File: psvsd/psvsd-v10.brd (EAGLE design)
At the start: 30 x 33.4 mm, 30 parts, among them J1 TRANSFLASH-PUSH, U1 USB2244QFN, U3 VREG, Y1 24.000MHz

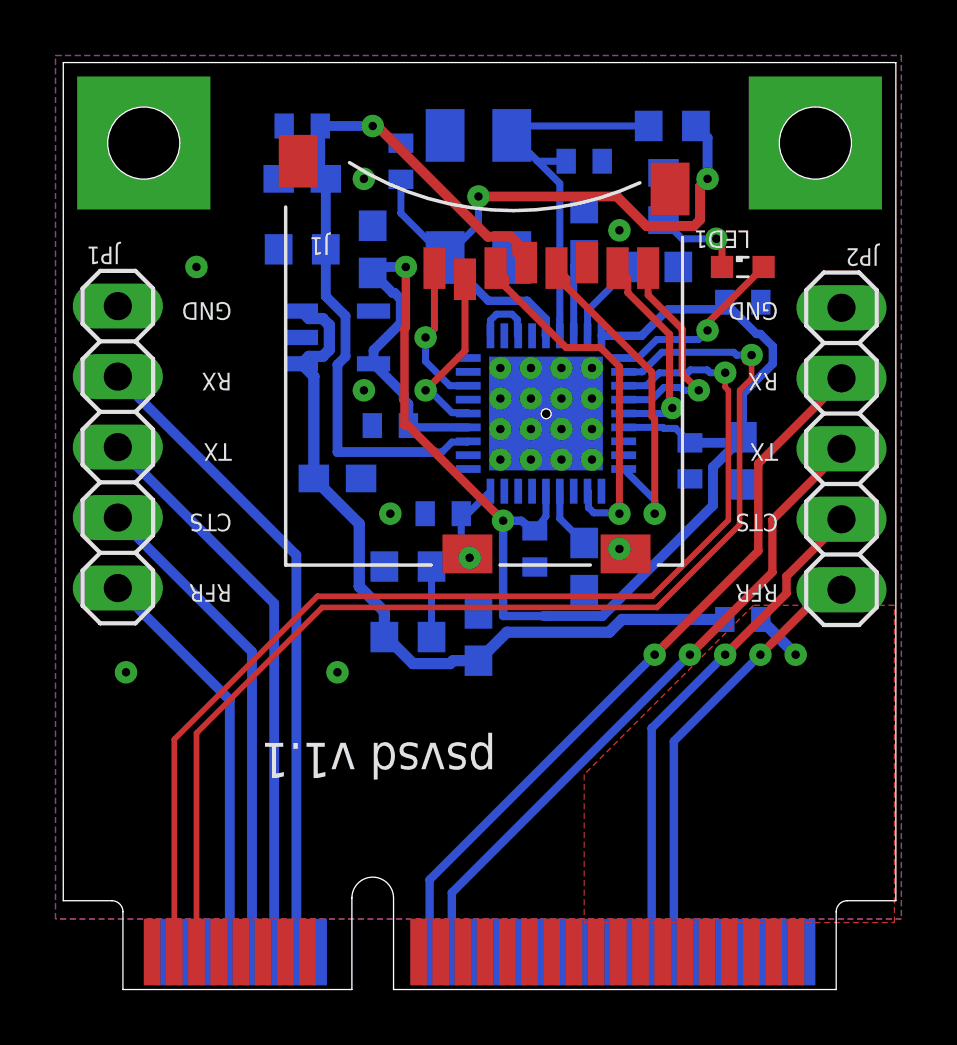
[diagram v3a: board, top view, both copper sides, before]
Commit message: Added MEM2051 part that will be used
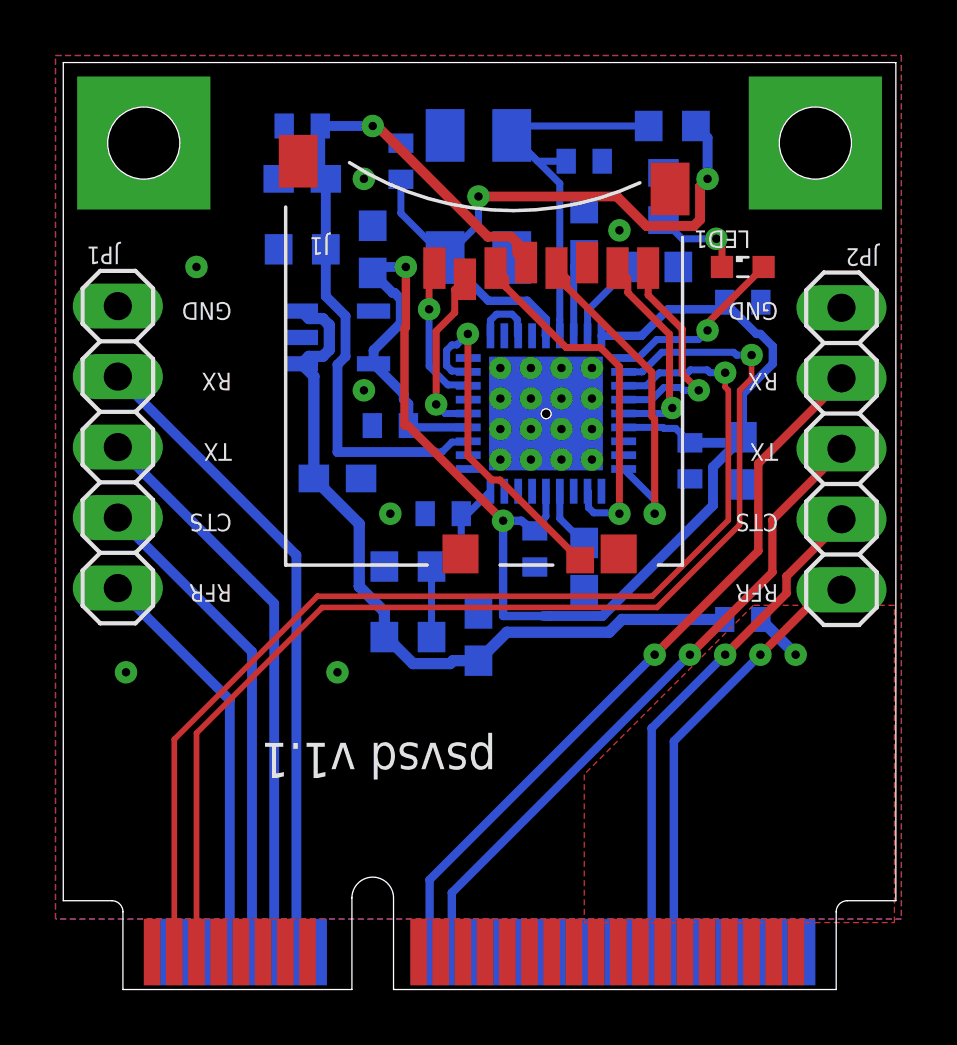
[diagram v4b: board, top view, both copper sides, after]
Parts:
- J1: value TRANSFLASH-PUSH -> MEM2051-00-195-00; device sd-mmc:MICROSD_MICROSD -> sd-mmc:MEM2051
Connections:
- new net !CD: J1.9, U1.26
- net GND: no longer J1.NC, J1.NC1, J1.NC2, J1.NC3
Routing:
- net !CD: track 0.00 -> 12.4 mm, vias 0 -> 1
- net GND: vias 25 -> 23

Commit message: Reconnected ground planes
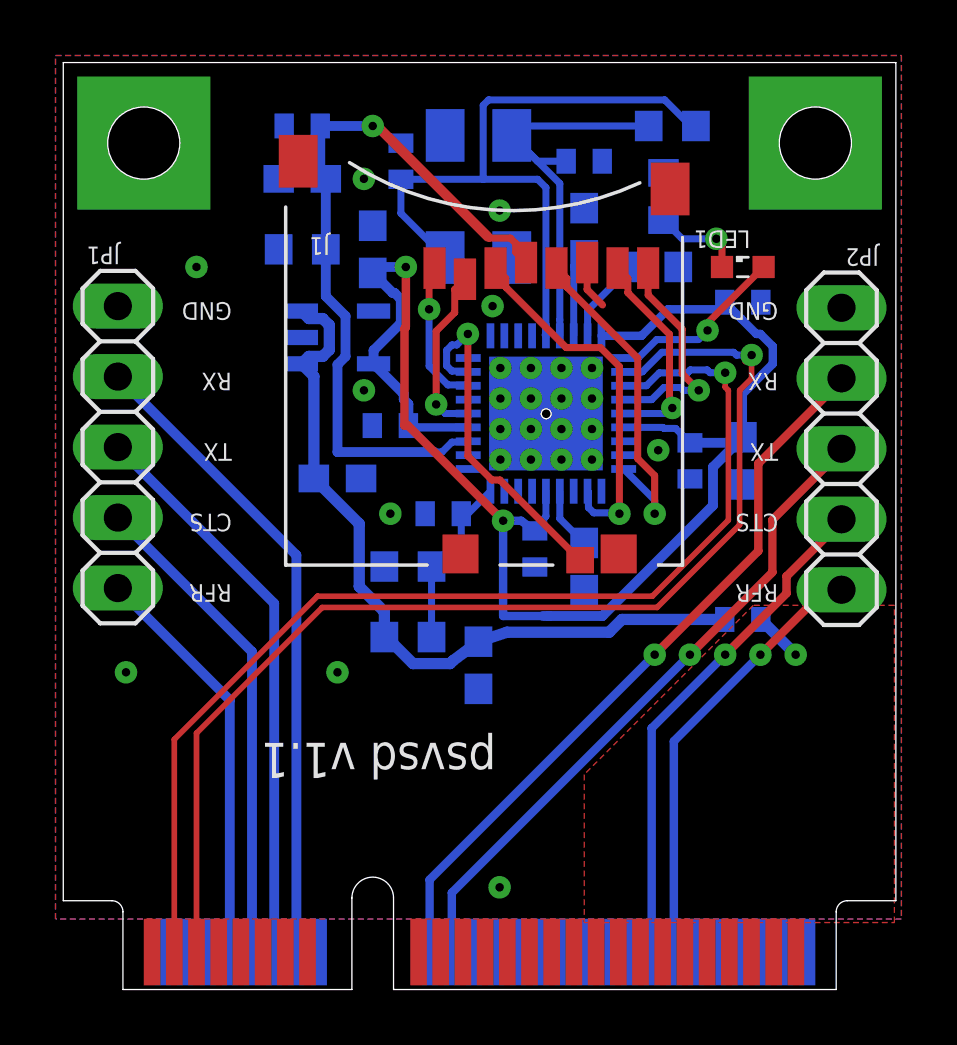
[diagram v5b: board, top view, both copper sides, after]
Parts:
- moved C5 1.02 mm to (16.5, 13.6), turned to 270 degrees
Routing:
- net XTAL2: track 23.5 -> 25.7 mm, vias 2 -> 0
- net GND: track 2.54 -> 2.00 mm, vias 23 -> 26
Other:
- board text added: "psvsd.henkaku.xyz"
